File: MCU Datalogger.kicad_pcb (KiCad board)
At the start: 2 copper layers, 37.1 x 30.2 mm, 29 parts, among them J2 ICSP, J3 Serial UART, J4 GPIO, U1 24LC1025, U2 24LC1025, Y1 32.768KHz, Y2 16 MHz

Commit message: done with 4 layer pcb design
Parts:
- moved Y2 0.78 mm to (34.4, 65.3)
- moved C3 0.52 mm to (34.4, 72.6)
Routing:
- net /VCC: track 128.4 -> 66.6 mm, vias 7 -> 9
- net /D8: track 10.4 -> 15.5 mm
- net Net-(U3-XTAL1/PB6): track 10.2 -> 15.1 mm, vias 0 -> 2
- net /SDA: track 40.3 -> 35.7 mm, vias 0 -> 4
- net /D3: track 26.3 -> 22.6 mm
- net /TX: track 20.4 -> 17.2 mm, vias 1 -> 0
- net /D4: track 23.2 -> 20.1 mm, vias 2 -> 0
- net /D7: track 10.5 -> 13.4 mm
- net /SCL: track 60.9 -> 63.6 mm
- net /RESET: track 18.5 -> 21.2 mm
- net /D2: track 29.5 -> 27.1 mm
- net GND: track 85.7 -> 83.4 mm
- net /RX: track 16.1 -> 18.4 mm, vias 2 -> 0
- net Net-(U3-XTAL2/PB7): track 8.81 -> 10.3 mm, vias 0 -> 2
- net Net-(U4-X1): track 10.2 -> 11.6 mm
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- added copper zone on In2.Cu, net /VCC
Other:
- copper layers 2 -> 4
- board text added: "Version 2: 4-Layer PCB"
- board text removed: "Version 1: 2-Layer PCB"

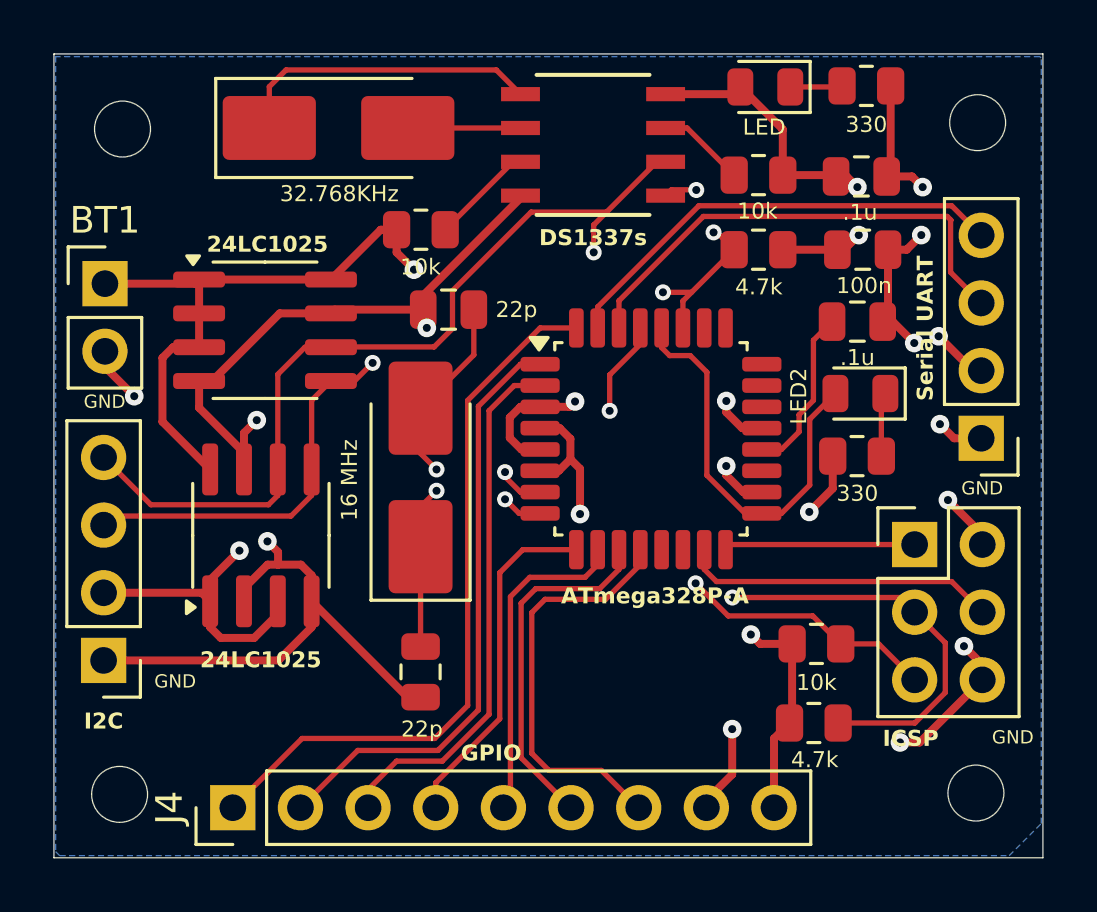
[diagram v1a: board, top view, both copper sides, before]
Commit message: finished wiring in 4layer
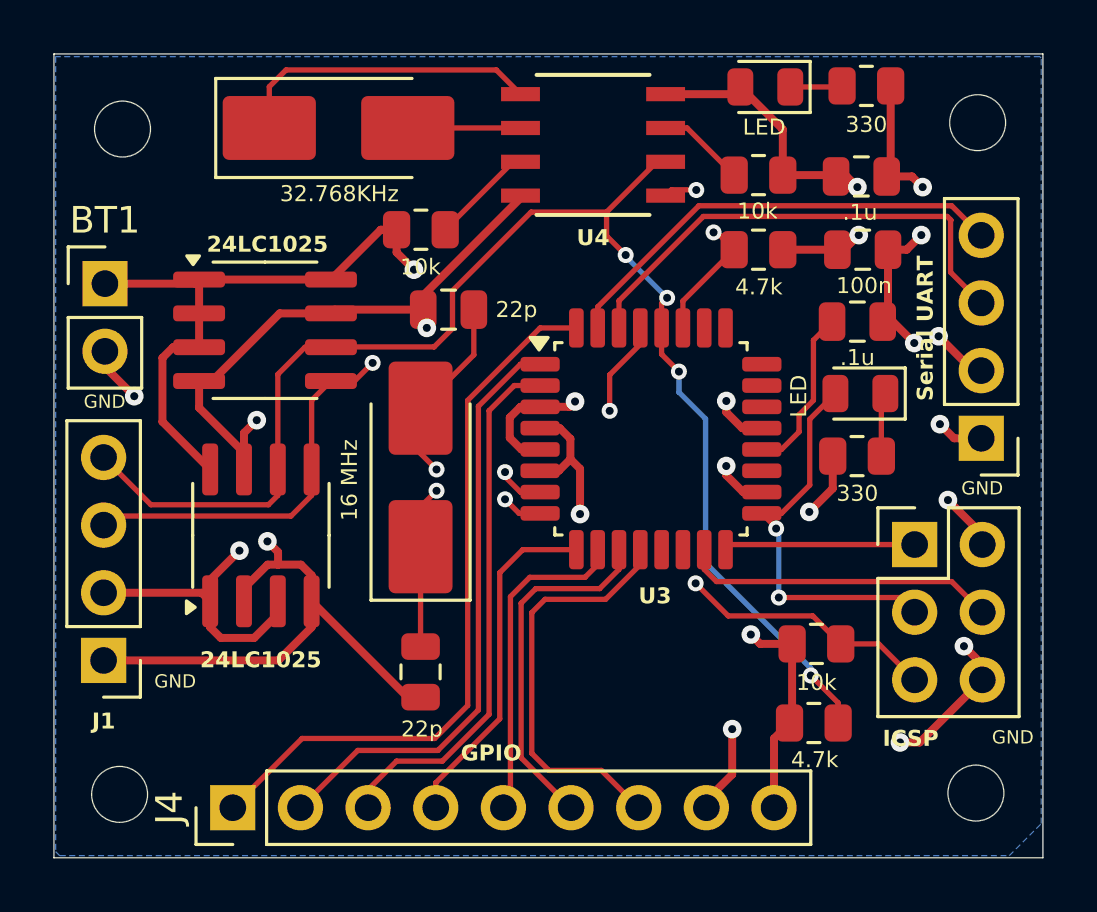
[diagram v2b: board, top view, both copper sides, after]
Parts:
- D2: value LED2 -> LED
- renumbered I2C to J1, ATmega328P-A to U3, DS1337s to U4
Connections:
- J2 pad 3: /SCL -> /SCK
- U3 pad 28: /SCK -> /SCL
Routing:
- net /SCL: track 63.6 -> 53.6 mm, vias 2 -> 4
- net /SDA: track 35.7 -> 37.4 mm, vias 4 -> 3
- net /SCK: track 15.4 -> 15.5 mm, vias 0 -> 2
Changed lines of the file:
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@@
 			)
 		)
-		(property "Value" "LED2"
+		(property "Value" "LED"
 			(at 2.3125 -0.1 270)
 			(layer "F.SilkS")
@@
 		(descr "TQFP, 32 Pin (JEDEC MS-026 variation ABA, https://www.jedec.org/document_search?search_api_views_fulltext=MS-026, https://ww1.microchip.com/downloads/en/PackagingSpec/00000049BZ.pdf#page=656), generated with kicad-footprint-generator ipc_gullwing_generator.py")
 		(tags "TQFP QFP")
-		(property "Reference" "ATmega328P-A"
+		(property "Reference" "U3"
 			(at 0.15 5.9 0)
 			(layer "F.SilkS")
@@
 			(layers "F.Cu" "F.Mask" "F.Paste")
 			(roundrect_rratio 0.25)
-			(net 8 "/SCK")
+			(net 9 "/SCL")
 			(pinfunction "PC5")
 			(pintype "bidirectional")
@@
 		(at 40.87585 52.815)
 		(tags "ds1337s+ ")
-		(property "Reference" "DS1337s"
+		(property "Reference" "U4"
 			(at 0 3.485 0)
 			(unlocked yes)
@@
 			(layers "*.Cu" "*.Mask")
 			(remove_unused_layers no)
-			(net 9 "/SCL")
+			(net 8 "/SCK")
 			(pinfunction "Pin_3")
 			(pintype "passive")
@@
 		(descr "Through hole straight pin header, 1x04, 2.54mm pitch, single row")
 		(tags "Through hole pin header THT 1x04 2.54mm single row")
-		(property "Reference" "I2C"
+		(property "Reference" "J1"
 			(at 0 -2.28 0)
 			(layer "F.SilkS")
@@
 	)
 	(segment
-		(start 43.45 59.6875)
-		(end 43.45 60.424999)
+		(start 49.0115 63.1135)
+		(end 49.975 62.15)
 		(width 0.2)
 		(layer "F.Cu")
@@
 	)
 	(segment
-		(start 49.0115 63.1135)
-		(end 49.975 62.15)
+		(start 47.75 67.22)
+		(end 47.75 67.1875)
 		(width 0.2)
 		(layer "F.Cu")
@@
 	)
 	(segment
-		(start 45.15 65.219654)
-		(end 46.580346 66.65)
+		(start 49.0115 65.588499)
+		(end 49.0115 63.1135)
 		(width 0.2)
 		(layer "F.Cu")
@@
 	)
 	(segment
-		(start 43.751001 60.726)
-		(end 44.526 60.726)
+		(start 47.2125 66.65)
+		(end 47.949999 66.65)
 		(width 0.2)
 		(layer "F.Cu")
@@
 	)
 	(segment
-		(start 49.0115 65.588499)
-		(end 49.0115 63.1135)
+		(start 46.580346 66.65)
+		(end 47.2125 66.65)
 		(width 0.2)
 		(layer "F.Cu")
@@
 	)
 	(segment
-		(start 45.15 61.35)
-		(end 45.15 65.219654)
+		(start 47.75 67.1875)
+		(end 47.2125 66.65)
 		(width 0.2)
 		(layer "F.Cu")
@@
 	)
 	(segment
-		(start 44.526 60.726)
-		(end 45.15 61.35)
+		(start 52.95 70.36)
+		(end 52.399 69.809)
 		(width 0.2)
 		(layer "F.Cu")
@@
 	)
 	(segment
-		(start 47.2125 66.65)
-		(end 47.949999 66.65)
+		(start 52.399 69.809)
+		(end 47.85 69.809)
 		(width 0.2)
 		(layer "F.Cu")
@@
 	)
 	(segment
-		(start 46.580346 66.65)
-		(end 47.2125 66.65)
+		(start 47.949999 66.65)
+		(end 49.0115 65.588499)
 		(width 0.2)
 		(layer "F.Cu")
 		(net 8)
 	)
+	(via
+		(at 47.75 67.22)
+		(size 0.6)
+		(drill 0.3)
+		(layers "F.Cu" "B.Cu")
+		(net 8)
+	)
+	(via
+		(at 47.85 69.809)
+		(size 0.6)
+		(drill 0.3)
+		(layers "F.Cu" "B.Cu")
+		(net 8)
+	)
 	(segment
-		(start 43.45 60.424999)
-		(end 43.751001 60.726)
+		(start 47.85 69.809)
+		(end 47.85 67.32)
 		(width 0.2)
-		(layer "F.Cu")
+		(layer "B.Cu")
 		(net 8)
 	)
 	(segment
-		(start 47.949999 66.65)
-		(end 49.0115 65.588499)
+		(start 47.85 67.32)
+		(end 47.75 67.22)
 		(width 0.2)
-		(layer "F.Cu")
+		(layer "B.Cu")
 		(net 8)
 	)
 	(segment
-		(start 40.9 56.85)
-		(end 40.9 55.82105)
+		(start 43.45 60.676)
+		(end 43.45 59.6875)
 		(width 0.2)
 		(layer "F.Cu")
@@
 	)
 	(segment
-		(start 52.95 70.36)
-		(end 52.399 69.809)
+		(start 44.1 61.326)
+		(end 43.45 60.676)
 		(width 0.2)
 		(layer "F.Cu")
@@
 	)
 	(segment
-		(start 54.101 71.511)
-		(end 52.95 70.36)
-		(width 0.2)
-		(layer "F.Cu")
-		(net 9)
-	)
-	(segment
 		(start 31.035 60.41)
 		(end 31.045 60.4)
@@
 	)
 	(segment
-		(start 54.101 73.37676)
-		(end 54.101 71.511)
+		(start 28.688999 66.326)
+		(end 24.276 66.326)
 		(width 0.2)
 		(layer "F.Cu")
@@
 	)
 	(segment
-		(start 28.688999 66.326)
-		(end 24.276 66.326)
+		(start 41.38335 55.3377)
+		(end 41.38335 56.23335)
 		(width 0.2)
 		(layer "F.Cu")
@@
 	)
 	(segment
-		(start 52.399 69.809)
-		(end 46.108999 69.809)
-		(width 0.2)
-		(layer "F.Cu")
-		(net 9)
-	)
-	(segment
 		(start 34.90916 60.4)
 		(end 35.599 59.71016)
@@
 	)
 	(segment
-		(start 52.95776 74.52)
-		(end 54.101 73.37676)
+		(start 43.45 59.6875)
+		(end 43.45 58.76416)
 		(width 0.2)
 		(layer "F.Cu")
@@
 	)
 	(segment
-		(start 40.9 55.82105)
-		(end 41.38335 55.3377)
-		(width 0.2)
-		(layer "F.Cu")
-		(net 9)
-	)
-	(segment
 		(start 29.04 65)
 		(end 29.04 61.430001)
@@
 	)
 	(segment
+		(start 41.38335 56.23335)
+		(end 42.1 56.95)
+		(width 0.2)
+		(layer "F.Cu")
+		(net 9)
+	)
+	(segment
 		(start 50.0775 74.52)
-		(end 52.95776 74.52)
+		(end 50.0775 73.76377)
+		(width 0.2)
+		(layer "F.Cu")
+		(net 9)
+	)
+	(segment
+		(start 43.45 58.76416)
+		(end 43.65708 58.55708)
 		(width 0.2)
 		(layer "F.Cu")
@@
 	)
 	(segment
+		(start 50.0775 73.76377)
+		(end 49.05 72.73627)
+		(width 0.2)
+		(layer "F.Cu")
+		(net 9)
+	)
+	(segment
 		(start 24.276 66.326)
 		(end 22.5 64.55)
@@
 	)
 	(via
-		(at 40.9 56.85)
+		(at 43.65708 58.55708)
 		(size 0.6)
 		(drill 0.3)
@@
 	)
 	(via
-		(at 46.108999 69.809)
+		(at 44.1 61.326)
+		(size 0.6)
+		(drill 0.3)
+		(layers "F.Cu" "B.Cu")
+		(net 9)
+	)
+	(via
+		(at 49.05 72.73627)
+		(size 0.6)
+		(drill 0.3)
+		(layers "F.Cu" "B.Cu")
+		(net 9)
+	)
+	(via
+		(at 42.1 56.95)
 		(size 0.6)
 		(drill 0.3)
@@
 	)
 	(segment
-		(start 40.9 56.85)
-		(end 40.9 63.049943)
+		(start 42.1 57)
+		(end 42.1 56.95)
 		(width 0.2)
-		(layer "In1.Cu")
+		(layer "B.Cu")
 		(net 9)
 	)
 	(segment
-		(start 40.9 63.049943)
-		(end 41.050028 63.199971)
+		(start 44.1 61.326)
+		(end 44.1 62.1)
 		(width 0.2)
-		(layer "In1.Cu")
+		(layer "B.Cu")
 		(net 9)
 	)
 	(segment
-		(start 46.040948 69.877051)
-		(end 46.108999 69.809)
+		(start 49.05 72.457636)
+		(end 49.05 72.73627)
 		(width 0.2)
-		(layer "In1.Cu")
+		(layer "B.Cu")
 		(net 9)
 	)
 	(segment
-		(start 41.050028 63.199971)
-		(end 41.050028 66.448499)
+		(start 43.65708 58.55708)
+		(end 42.1 57)
 		(width 0.2)
-		(layer "In1.Cu")
+		(layer "B.Cu")
 		(net 9)
 	)
 	(segment
-		(start 41.050028 66.448499)
-		(end 44.47858 69.877051)
+		(start 45.1 63.1)
+		(end 45.1 68.507636)
 		(width 0.2)
-		(layer "In1.Cu")
+		(layer "B.Cu")
 		(net 9)
 	)
 	(segment
-		(start 44.47858 69.877051)
-		(end 46.040948 69.877051)
+		(start 45.1 68.507636)
+		(end 49.05 72.457636)
 		(width 0.2)
-		(layer "In1.Cu")
+		(layer "B.Cu")
+		(net 9)
+	)
+	(segment
+		(start 44.1 62.1)
+		(end 45.1 63.1)
+		(width 0.2)
+		(layer "B.Cu")
 		(net 9)
 	)
@@
 	)
 	(segment
-		(start 43.5 58.35)
-		(end 44.575 58.35)
-		(width 0.2)
-		(layer "F.Cu")
-		(net 10)
-	)
-	(segment
 		(start 44.75136 54.508163)
 		(end 44.743197 54.5)
@@
 		(net 10)
 	)
-	(via
-		(at 43.5 58.35)
-		(size 0.6)
-		(drill 0.3)
-		(layers "F.Cu" "B.Cu")
-		(net 10)
-	)
 	(segment
 		(start 44.75136 54.508163)
@@
 	)
 	(segment
+		(start 45.26463 56.101)
+		(end 45.4 56.101)
+		(width 0.2)
+		(layer "In2.Cu")
+		(net 10)
+	)
+	(segment
 		(start 32.6 61)
-		(end 40.85 61)
+		(end 40.36563 61)
 		(width 0.2)
 		(layer "In2.Cu")
@@
 	)
 	(segment
-		(start 40.85 61)
-		(end 43.5 58.35)
+		(start 40.36563 61)
+		(end 45.26463 56.101)
 		(width 0.2)
 		(layer "In2.Cu")
